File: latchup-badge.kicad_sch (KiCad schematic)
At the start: 49 parts, among them J1 USB_C_Receptacle_USB2.0, J2 Connector_Generic:Conn_02x06_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, J3 Connector_Generic:Conn_02x06_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, J4 Connector_Generic:Conn_02x05_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, J5 Connector_Generic:Conn_02x06_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, SW1 SW_Push, SW2 SW_Push, U1 ICE40UP5K-SG48ITR, U2 TLV70012_SOT23-5, U3 TLV70033_SOT23-5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

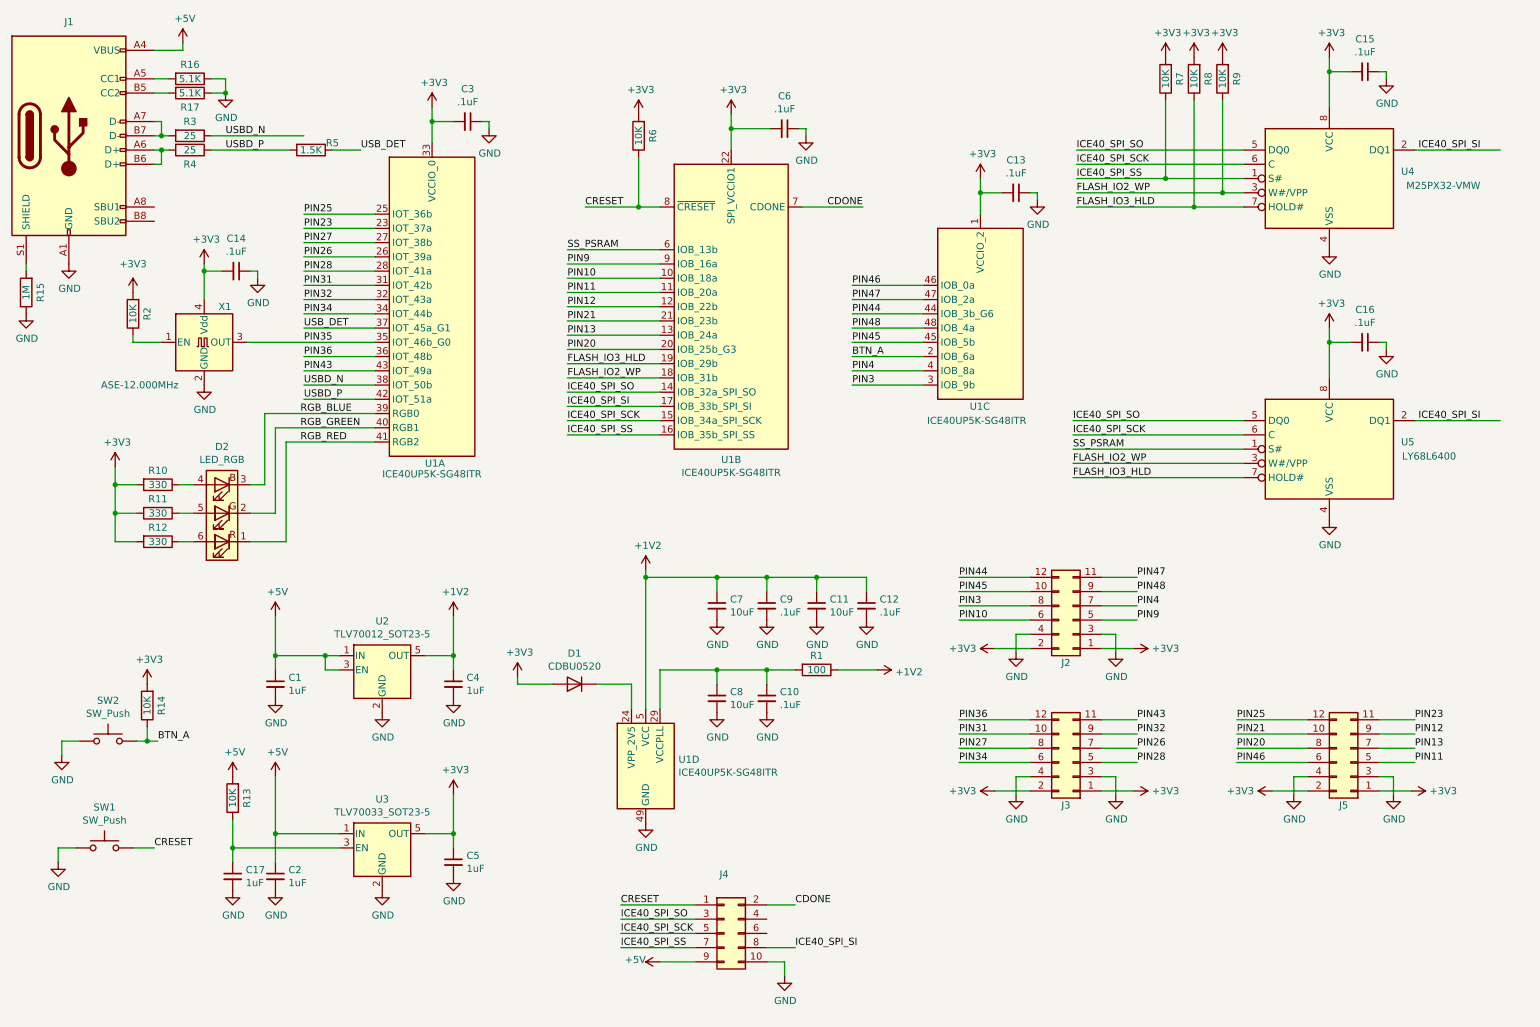
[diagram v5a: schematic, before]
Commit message: Add series damping resistors on PMODs
Signed-off-by: Michael Welling <mwelling@ieee.org>
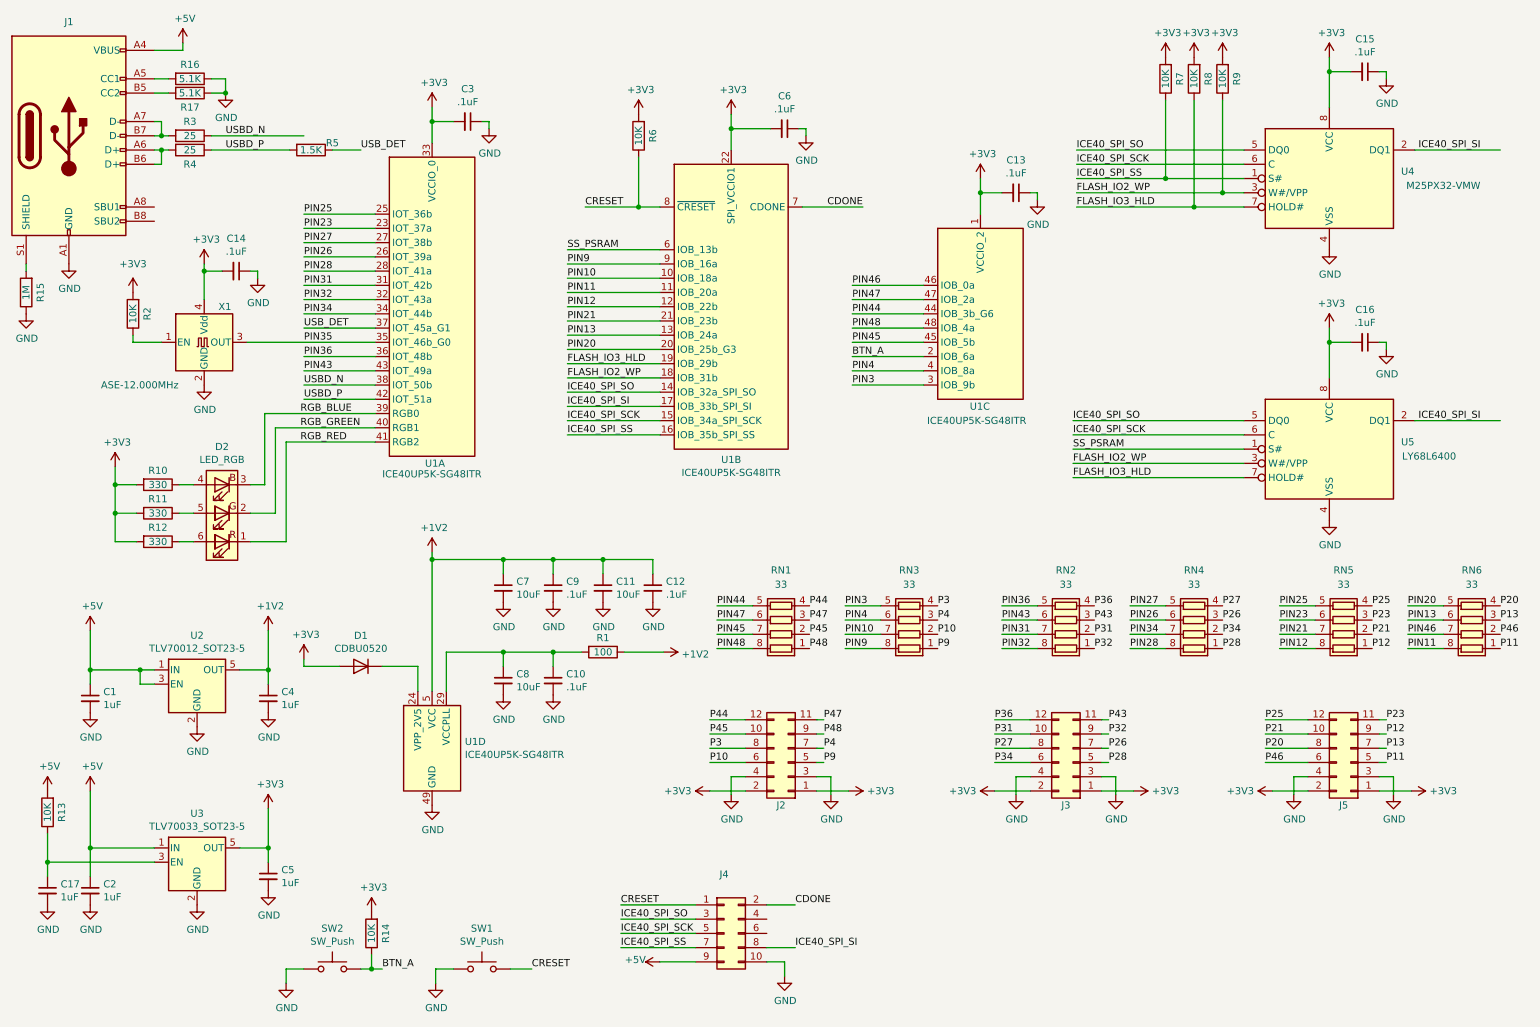
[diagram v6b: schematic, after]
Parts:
- added RN1, RN2, RN3, RN4, RN5, RN6: 33, Resistor_SMD:R_Array_Concave_4x0402, symbol Device:R_Pack04
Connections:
- net PIN10: now also RN3.7 (R2.2); no longer J2.6 (Pin_6)
- net PIN11: now also RN6.8 (R1.2); no longer J5.5 (Pin_5)
- net PIN12: now also RN5.8 (R1.2); no longer J5.9 (Pin_9)
- net PIN13: now also RN6.6 (R3.2); no longer J5.7 (Pin_7)
- net PIN20: now also RN6.5 (R4.2); no longer J5.8 (Pin_8)
- net PIN21: now also RN5.7 (R2.2); no longer J5.10 (Pin_10)
- net PIN23: now also RN5.6 (R3.2); no longer J5.11 (Pin_11)
- net PIN25: now also RN5.5 (R4.2); no longer J5.12 (Pin_12)
- net PIN26: now also RN4.6 (R3.2); no longer J3.7 (Pin_7)
- net PIN27: now also RN4.5 (R4.2); no longer J3.8 (Pin_8)
- net PIN28: now also RN4.8 (R1.2); no longer J3.5 (Pin_5)
- net PIN3: now also RN3.5 (R4.2); no longer J2.8 (Pin_8)
- net PIN31: now also RN2.7 (R2.2); no longer J3.10 (Pin_10)
- net PIN32: now also RN2.8 (R1.2); no longer J3.9 (Pin_9)
- net PIN34: now also RN4.7 (R2.2); no longer J3.6 (Pin_6)
- net PIN36: now also RN2.5 (R4.2); no longer J3.12 (Pin_12)
- net PIN4: now also RN3.6 (R3.2); no longer J2.7 (Pin_7)
- net PIN43: now also RN2.6 (R3.2); no longer J3.11 (Pin_11)
- net PIN44: now also RN1.5 (R4.2); no longer J2.12 (Pin_12)
- net PIN45: now also RN1.7 (R2.2); no longer J2.10 (Pin_10)
- net PIN46: now also RN6.7 (R2.2); no longer J5.6 (Pin_6)
- net PIN47: now also RN1.6 (R3.2); no longer J2.11 (Pin_11)
- net PIN48: now also RN1.8 (R1.2); no longer J2.9 (Pin_9)
- net PIN9: now also RN3.8 (R1.2); no longer J2.5 (Pin_5)
- new net P10: J2.6 (Pin_6), RN3.2 (R2.1)
- new net P11: J5.5 (Pin_5), RN6.1 (R1.1)
- new net P12: J5.9 (Pin_9), RN5.1 (R1.1)
- new net P13: J5.7 (Pin_7), RN6.3 (R3.1)
- new net P20: J5.8 (Pin_8), RN6.4 (R4.1)
- new net P21: J5.10 (Pin_10), RN5.2 (R2.1)
- new net P23: J5.11 (Pin_11), RN5.3 (R3.1)
- new net P25: J5.12 (Pin_12), RN5.4 (R4.1)
- new net P26: J3.7 (Pin_7), RN4.3 (R3.1)
- new net P27: J3.8 (Pin_8), RN4.4 (R4.1)
- new net P28: J3.5 (Pin_5), RN4.1 (R1.1)
- new net P3: J2.8 (Pin_8), RN3.4 (R4.1)
- new net P31: J3.10 (Pin_10), RN2.2 (R2.1)
- new net P32: J3.9 (Pin_9), RN2.1 (R1.1)
- new net P34: J3.6 (Pin_6), RN4.2 (R2.1)
- new net P36: J3.12 (Pin_12), RN2.4 (R4.1)
- new net P4: J2.7 (Pin_7), RN3.3 (R3.1)
- new net P43: J3.11 (Pin_11), RN2.3 (R3.1)
- new net P44: J2.12 (Pin_12), RN1.4 (R4.1)
- new net P45: J2.10 (Pin_10), RN1.2 (R2.1)
- new net P46: J5.6 (Pin_6), RN6.2 (R2.1)
- new net P47: J2.11 (Pin_11), RN1.3 (R3.1)
- new net P48: J2.9 (Pin_9), RN1.1 (R1.1)
- new net P9: J2.5 (Pin_5), RN3.1 (R1.1)
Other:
- moved on the sheet: C1, C10, C11, C12, C17, C2, C4, C5, C7, C8, C9, D1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
